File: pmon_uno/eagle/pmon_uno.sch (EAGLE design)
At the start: 42 parts, among them J1 USB, J2 USB, J3 TERMINAL-2, U1 LTC2943, U2 FT232RL, U3 LT1764AEQ, U4 ATMEGA328TQFP32

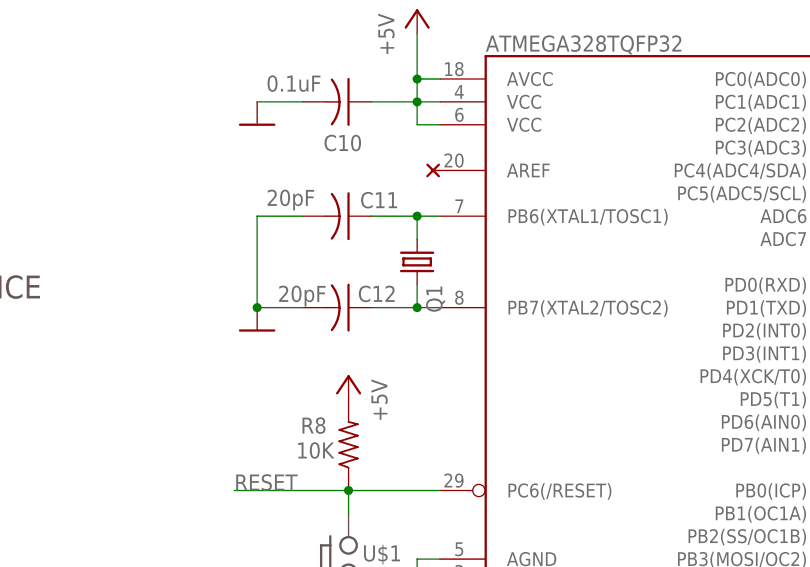
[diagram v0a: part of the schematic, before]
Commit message: Replaced dipswitch to through hole. Undone auto routing.
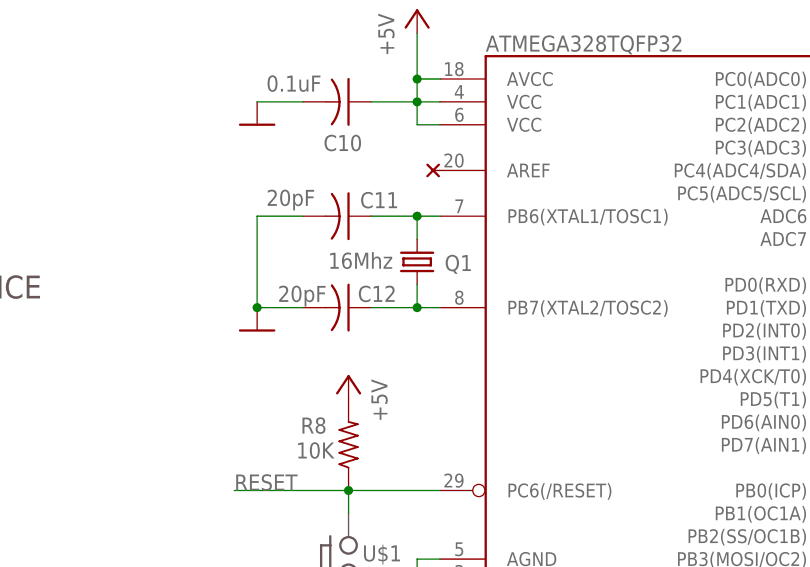
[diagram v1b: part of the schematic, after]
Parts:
- C1, C3, C6: device powermon:CPOL-USA/3216-18R -> pmon_uno:CPOL-USA/3216-18R
- C10, C11, C12, C2, C4, C5, C7, C8, C9: device powermon:C-USC0603 -> pmon_uno:C-USC0603
- D1, D2, D3, D4, D5: device powermon:LED -> pmon_uno:LED
- J1, J2: device powermon:USB -> pmon_uno:USB
- J3: device powermon:TERMINAL-2 -> pmon_uno:TERMINAL-2
- J4: device powermon:PINHD-2X3 -> pmon_uno:PINHD-2X3
- PCB1: device powermon:PCB_DP_SQUARE-5X5 -> pmon_uno:PCB_DP_SQUARE-5X5
- Q1: value (none) -> 16Mhz; device powermon:CRYSTALCTS406 -> pmon_uno:CRYSTALCTS406
- R1, R10, R11, R12, R13, R2, R3, R6, R7, R8, R9: device powermon:R-US_R0603 -> pmon_uno:R-US_R0603
- R4: device powermon:SHUNT -> pmon_uno:SHUNT
- R5: device powermon:TRIM_US-SM-42/43A -> pmon_uno:TRIM_US-SM-42/43A
- S1: device powermon:PUSH_BUTTONEVQPSL -> pmon_uno:PUSH_BUTTONEVQPSL
- S2: value 219-04 -> DIP_SWITCH-X4; device powermon:219-04 -> pmon_uno:DIP_SWITCH-X4
- U1: device powermon:LTC2943 -> pmon_uno:LTC2943
- U2: device powermon:FT232RL -> pmon_uno:FT232RL
- U3: device powermon:LTE1764 -> pmon_uno:LTE1764
- U4: device powermon:ATMEGA328TQFP32 -> pmon_uno:ATMEGA328TQFP32

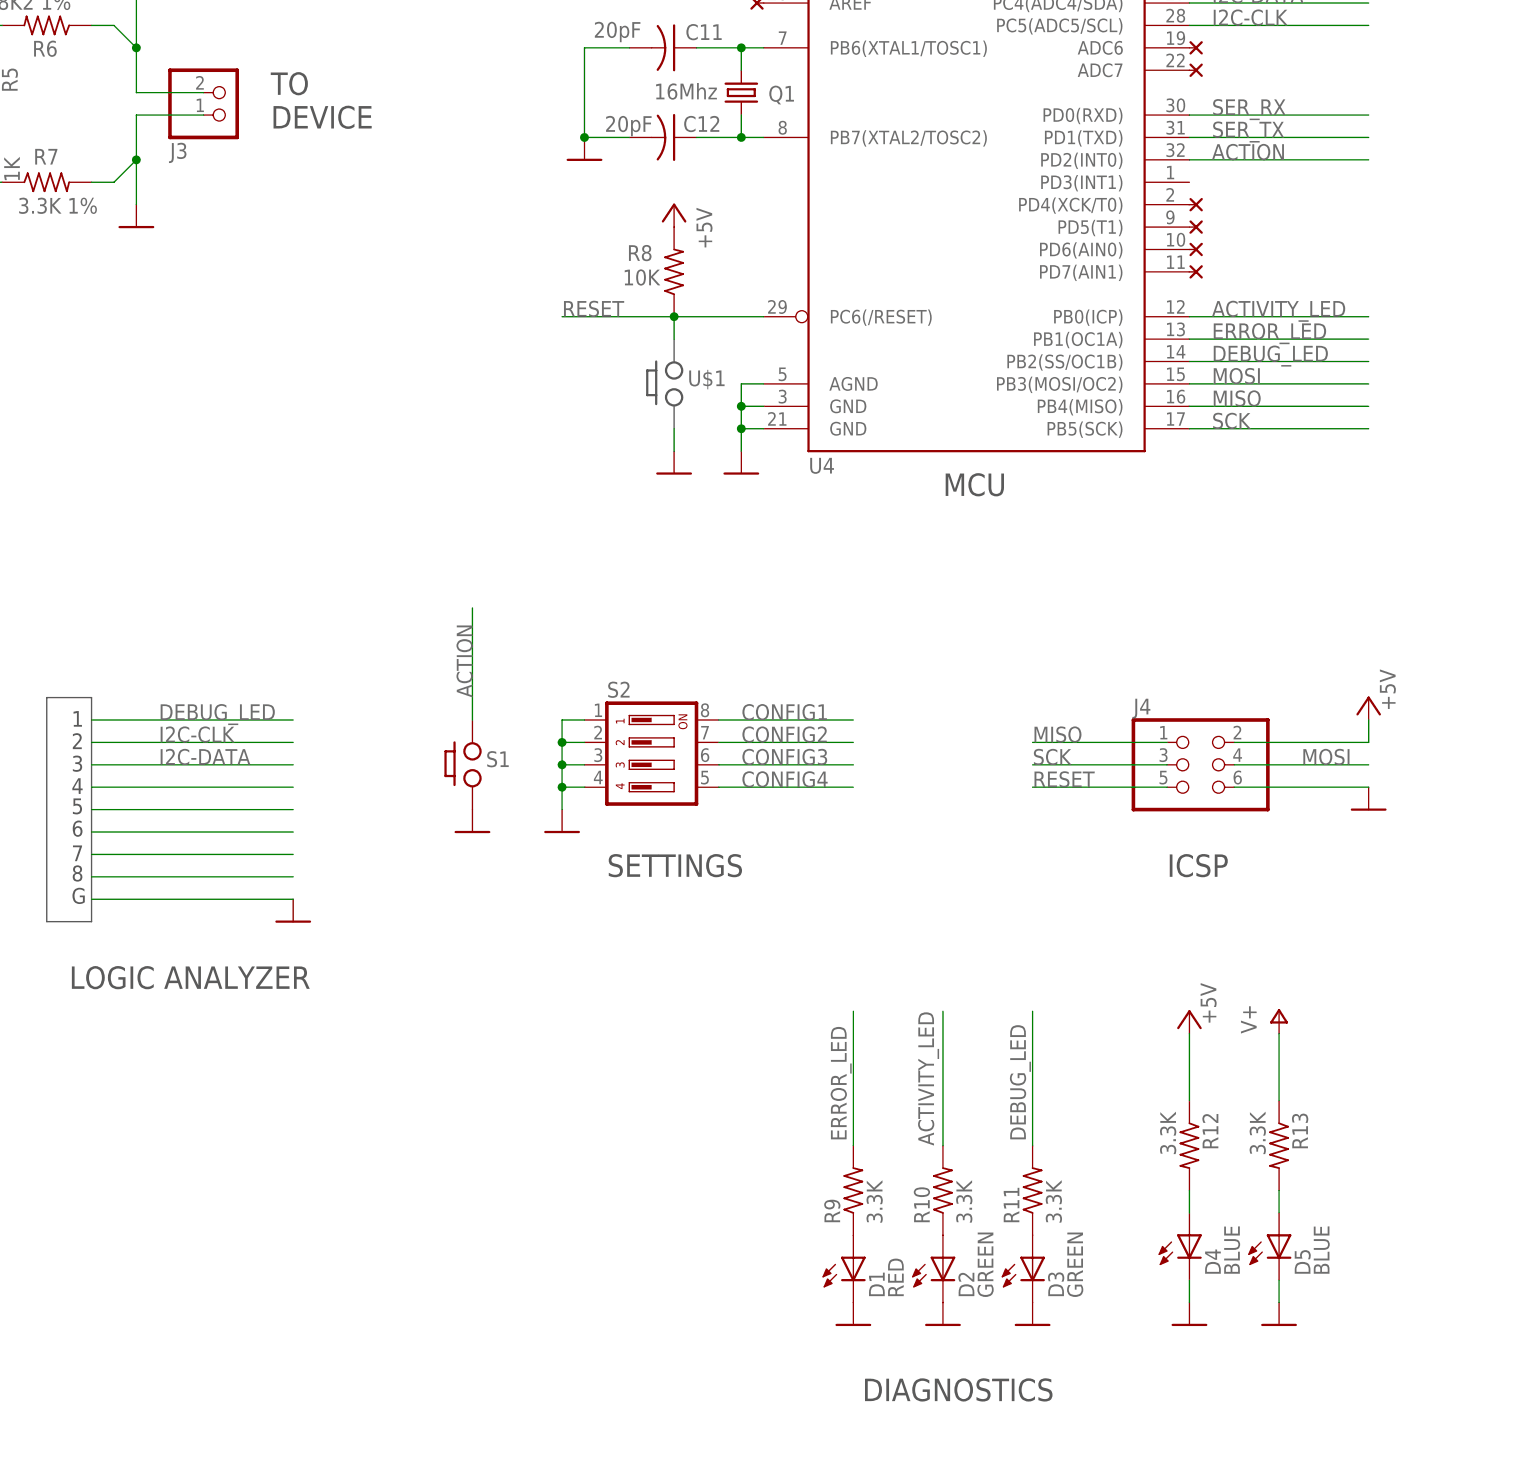
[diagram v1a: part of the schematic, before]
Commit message: Rearanged the leds pin to have a PWM option for the Status led.
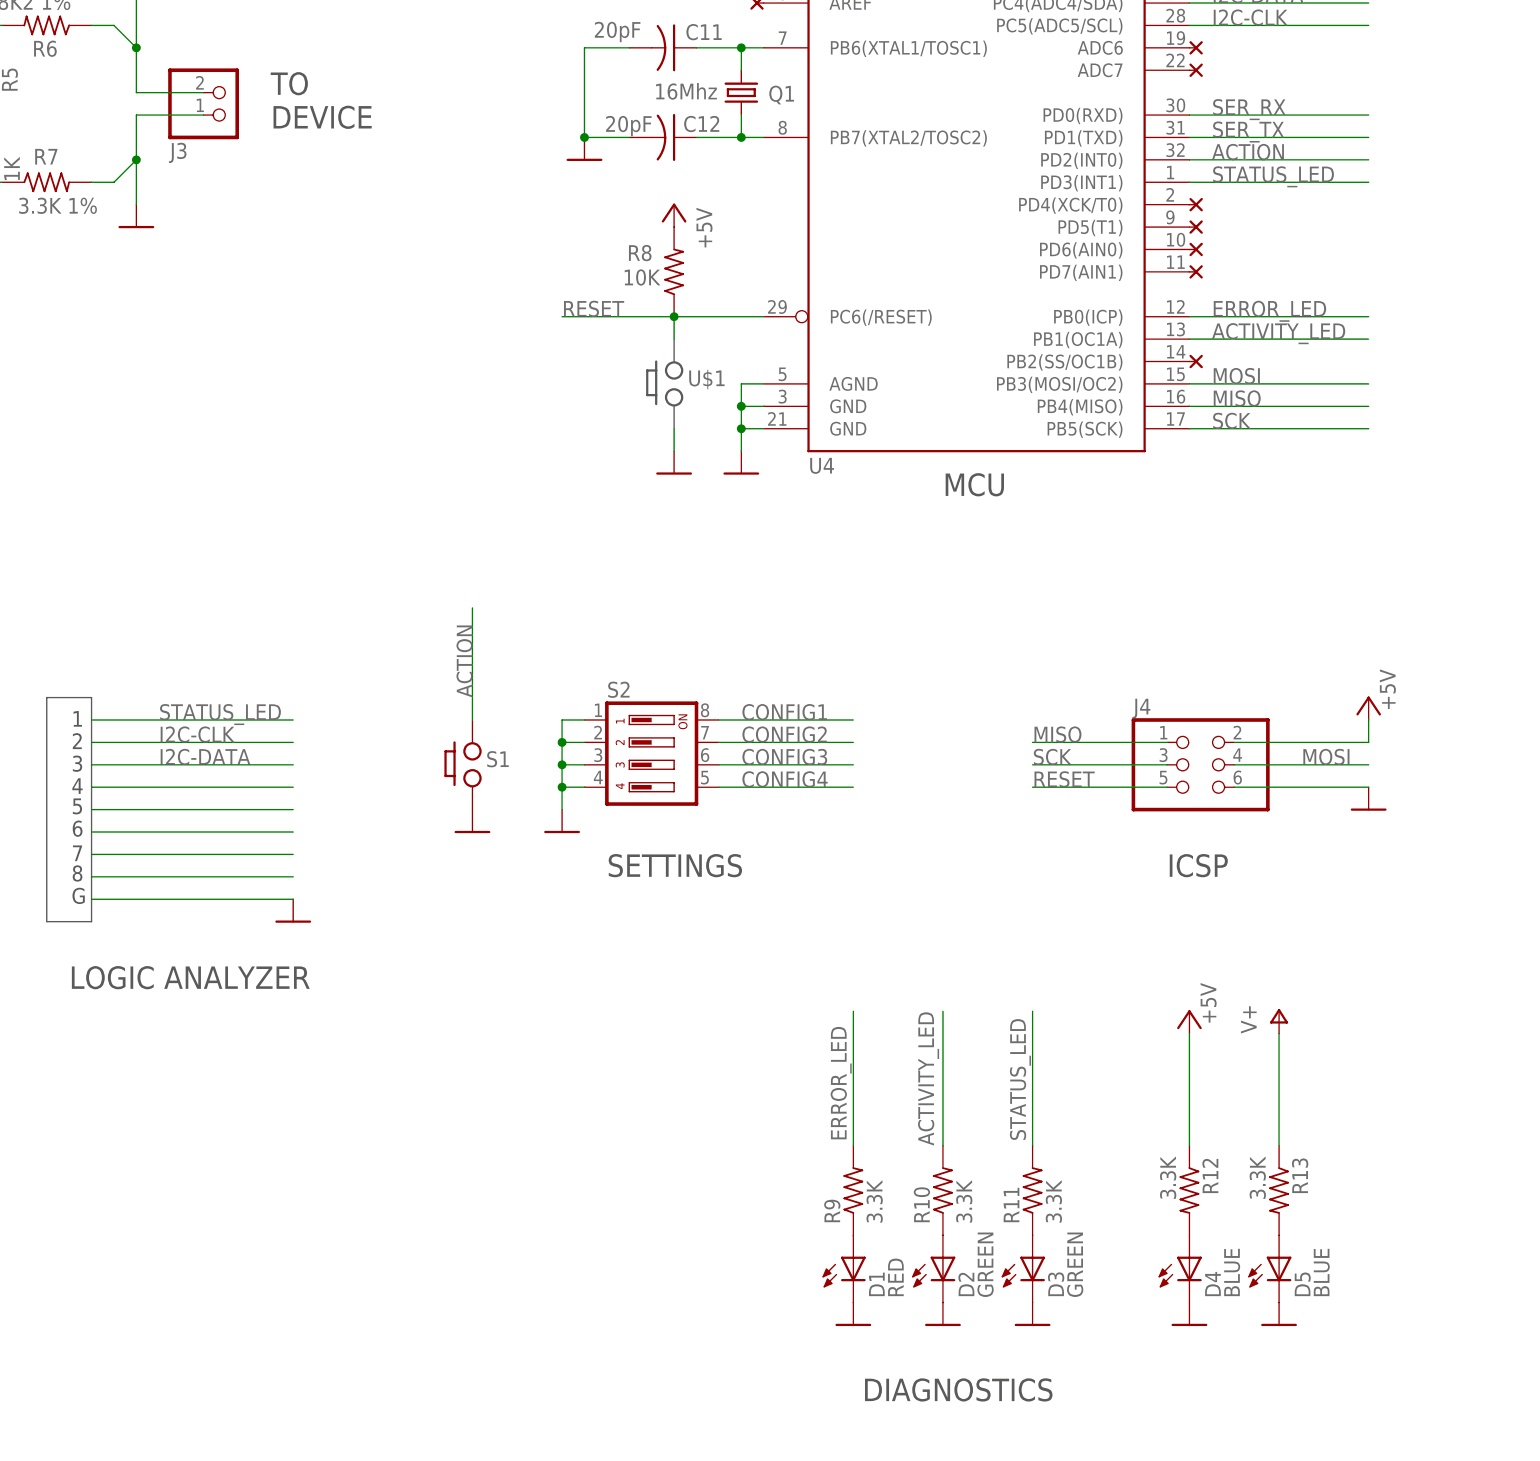
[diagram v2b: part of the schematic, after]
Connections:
- removed net DEBUG_LED: R11.2, U4.PB2(SS/OC1B)
- new net STATUS_LED: R11.2, U4.PD3(INT1)
- net ACTIVITY_LED: now also U4.PB1(OC1A); no longer U4.PB0(ICP)
- net ERROR_LED: now also U4.PB0(ICP); no longer U4.PB1(OC1A)
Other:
- moved on the sheet: D4, D5, R12, R13
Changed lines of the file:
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@@
 <part name="U$7" library="pmon_uno" deviceset="NC" device=""/>
 <part name="U$8" library="pmon_uno" deviceset="NC" device=""/>
+<part name="U$9" library="pmon_uno" deviceset="NC" device=""/>
 </parts>
 <sheets>
@@
 <instance part="C3" gate="G$1" x="17.78" y="45.72"/>
 <instance part="GND1" gate="1" x="170.18" y="208.28" rot="MR0"/>
-<instance part="D4" gate="G$1" x="238.76" y="63.5"/>
-<instance part="R12" gate="G$1" x="238.76" y="73.66" rot="R270"/>
+<instance part="D4" gate="G$1" x="238.76" y="60.96"/>
+<instance part="R12" gate="G$1" x="238.76" y="68.58" rot="R270"/>
 <instance part="P+4" gate="1" x="91.44" y="86.36" smashed="yes" rot="MR90">
 <attribute name="VALUE" x="82.804" y="88.646" size="1.778" layer="96" rot="MR180"/>
@@
 <instance part="U1" gate="G$1" x="38.1" y="129.54"/>
 <instance part="GND17" gate="1" x="17.78" y="111.76"/>
-<instance part="D5" gate="G$1" x="248.92" y="63.5"/>
-<instance part="R13" gate="G$1" x="248.92" y="73.66" rot="R270"/>
+<instance part="D5" gate="G$1" x="248.92" y="60.96"/>
+<instance part="R13" gate="G$1" x="248.92" y="68.58" rot="R270"/>
 <instance part="GND28" gate="1" x="248.92" y="53.34" rot="MR0"/>
 <instance part="P+8" gate="1" x="248.92" y="88.9"/>
@@
 <instance part="U$7" gate="G$1" x="2.54" y="205.74" rot="R180"/>
 <instance part="U$8" gate="G$1" x="2.54" y="203.2" rot="R180"/>
+<instance part="U$9" gate="G$1" x="238.76" y="162.56" rot="R180"/>
 </instances>
 <busses>
@@
 <pinref part="D4" gate="G$1" pin="C"/>
 <pinref part="GND18" gate="1" pin="GND"/>
-<wire x1="238.76" y1="55.88" x2="238.76" y2="58.42" width="0.1524" layer="91"/>
 </segment>
 <segment>
@@
 <pinref part="D5" gate="G$1" pin="C"/>
 <pinref part="GND28" gate="1" pin="GND"/>
-<wire x1="248.92" y1="55.88" x2="248.92" y2="58.42" width="0.1524" layer="91"/>
 </segment>
 <segment>
@@
 <segment>
 <pinref part="R12" gate="G$1" pin="1"/>
-<wire x1="238.76" y1="86.36" x2="238.76" y2="78.74" width="0.1524" layer="91"/>
+<wire x1="238.76" y1="86.36" x2="238.76" y2="73.66" width="0.1524" layer="91"/>
 <pinref part="P+3" gate="1" pin="+5V"/>
 </segment>
@@
 </segment>
 <segment>
-<wire x1="238.76" y1="165.1" x2="259.08" y2="165.1" width="0.1524" layer="91"/>
-<label x="241.3" y="165.1" size="1.778" layer="95"/>
-<pinref part="U4" gate="G$1" pin="PB1(OC1A)"/>
+<pinref part="U4" gate="G$1" pin="PB0(ICP)"/>
+<wire x1="238.76" y1="167.64" x2="259.08" y2="167.64" width="0.1524" layer="91"/>
+<label x="241.3" y="167.64" size="1.778" layer="95"/>
 </segment>
 </net>
@@
 <pinref part="D4" gate="G$1" pin="A"/>
 <pinref part="R12" gate="G$1" pin="2"/>
-<wire x1="238.76" y1="68.58" x2="238.76" y2="66.04" width="0.1524" layer="91"/>
 </segment>
 </net>
@@
 <net name="ACTIVITY_LED" class="0">
 <segment>
-<wire x1="238.76" y1="167.64" x2="259.08" y2="167.64" width="0.1524" layer="91"/>
-<label x="241.3" y="167.64" size="1.778" layer="95"/>
-<pinref part="U4" gate="G$1" pin="PB0(ICP)"/>
-</segment>
-<segment>
 <pinref part="R10" gate="G$1" pin="2"/>
 <wire x1="210.82" y1="88.9" x2="210.82" y2="73.66" width="0.1524" layer="91"/>
 <label x="209.804" y="73.66" size="1.778" layer="95" rot="R90"/>
+</segment>
+<segment>
+<pinref part="U4" gate="G$1" pin="PB1(OC1A)"/>
+<wire x1="238.76" y1="165.1" x2="259.08" y2="165.1" width="0.1524" layer="91"/>
+<label x="241.3" y="165.1" size="1.778" layer="95"/>
 </segment>
 </net>
@@
 <segment>
 <pinref part="R13" gate="G$1" pin="1"/>
-<wire x1="248.92" y1="86.36" x2="248.92" y2="78.74" width="0.1524" layer="91"/>
+<wire x1="248.92" y1="86.36" x2="248.92" y2="73.66" width="0.1524" layer="91"/>
 <pinref part="P+8" gate="1" pin="V+"/>
 </segment>
@@
 <pinref part="D5" gate="G$1" pin="A"/>
 <pinref part="R13" gate="G$1" pin="2"/>
-<wire x1="248.92" y1="68.58" x2="248.92" y2="66.04" width="0.1524" layer="91"/>
 </segment>
 </net>
@@
 </segment>
 </net>
-<net name="DEBUG_LED" class="0">
+<net name="STATUS_LED" class="0">
 <segment>
 <pinref part="R11" gate="G$1" pin="2"/>
@@
 </segment>
 <segment>
-<wire x1="238.76" y1="162.56" x2="259.08" y2="162.56" width="0.1524" layer="91"/>
-<label x="241.3" y="162.56" size="1.778" layer="95"/>
-<pinref part="U4" gate="G$1" pin="PB2(SS/OC1B)"/>
-</segment>
-<segment>
 <wire x1="114.3" y1="121.92" x2="137.16" y2="121.92" width="0.1524" layer="91"/>
 <label x="121.92" y="121.92" size="1.778" layer="95"/>
 </segment>
-</net>
+<segment>
+<pinref part="U4" gate="G$1" pin="PD3(INT1)"/>
+<wire x1="238.76" y1="182.88" x2="259.08" y2="182.88" width="0.1524" layer="91"/>
+<label x="241.3" y="182.88" size="1.778" layer="95"/>
+</segment>
+</net>

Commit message: Layout completed.
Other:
- note added: "(ARDUINO MINI PRO 328P 5V 16Mhz)"
- note added: "* PROTOTYPE ONLY"
- note added: "Arduino Single Cell Battery Power Monitor"
- note added: "C/V/A SENSE"
- note added: "LOGIC ANALYZER *"
- note added: "RESET*"
- note removed: "Battery Power Monitor"
- note removed: "LOGIC ANALYZER"
- note removed: "V/A SENSE"
- moved on the sheet: C2, D1, D2, D3, D4, D5, R1, R10, R11, R12, R13, R2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
